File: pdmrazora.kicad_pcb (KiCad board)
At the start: 2 copper layers, 174 x 202 mm, 54 parts, among them J1 6473418-1, J2 M6_VBAT, J3 M6_GND, M1000 Module:mega-mcu144/0.7, U1 BTS50010-1TAD, U11 BTS7004-1EPP, U12 BTS7004-1EPP, U13 BTS7004-1EPP, U14 BTS7004-1EPP, U15 BTS7004-1EPP, U16 BTS7004-1EPP, U17 BTS7004-1EPP, U18 BTS7004-1EPP, U2 BTS50010-1TAD, U3 BTS50010-1TAD, U4 BTS50010-1TAD

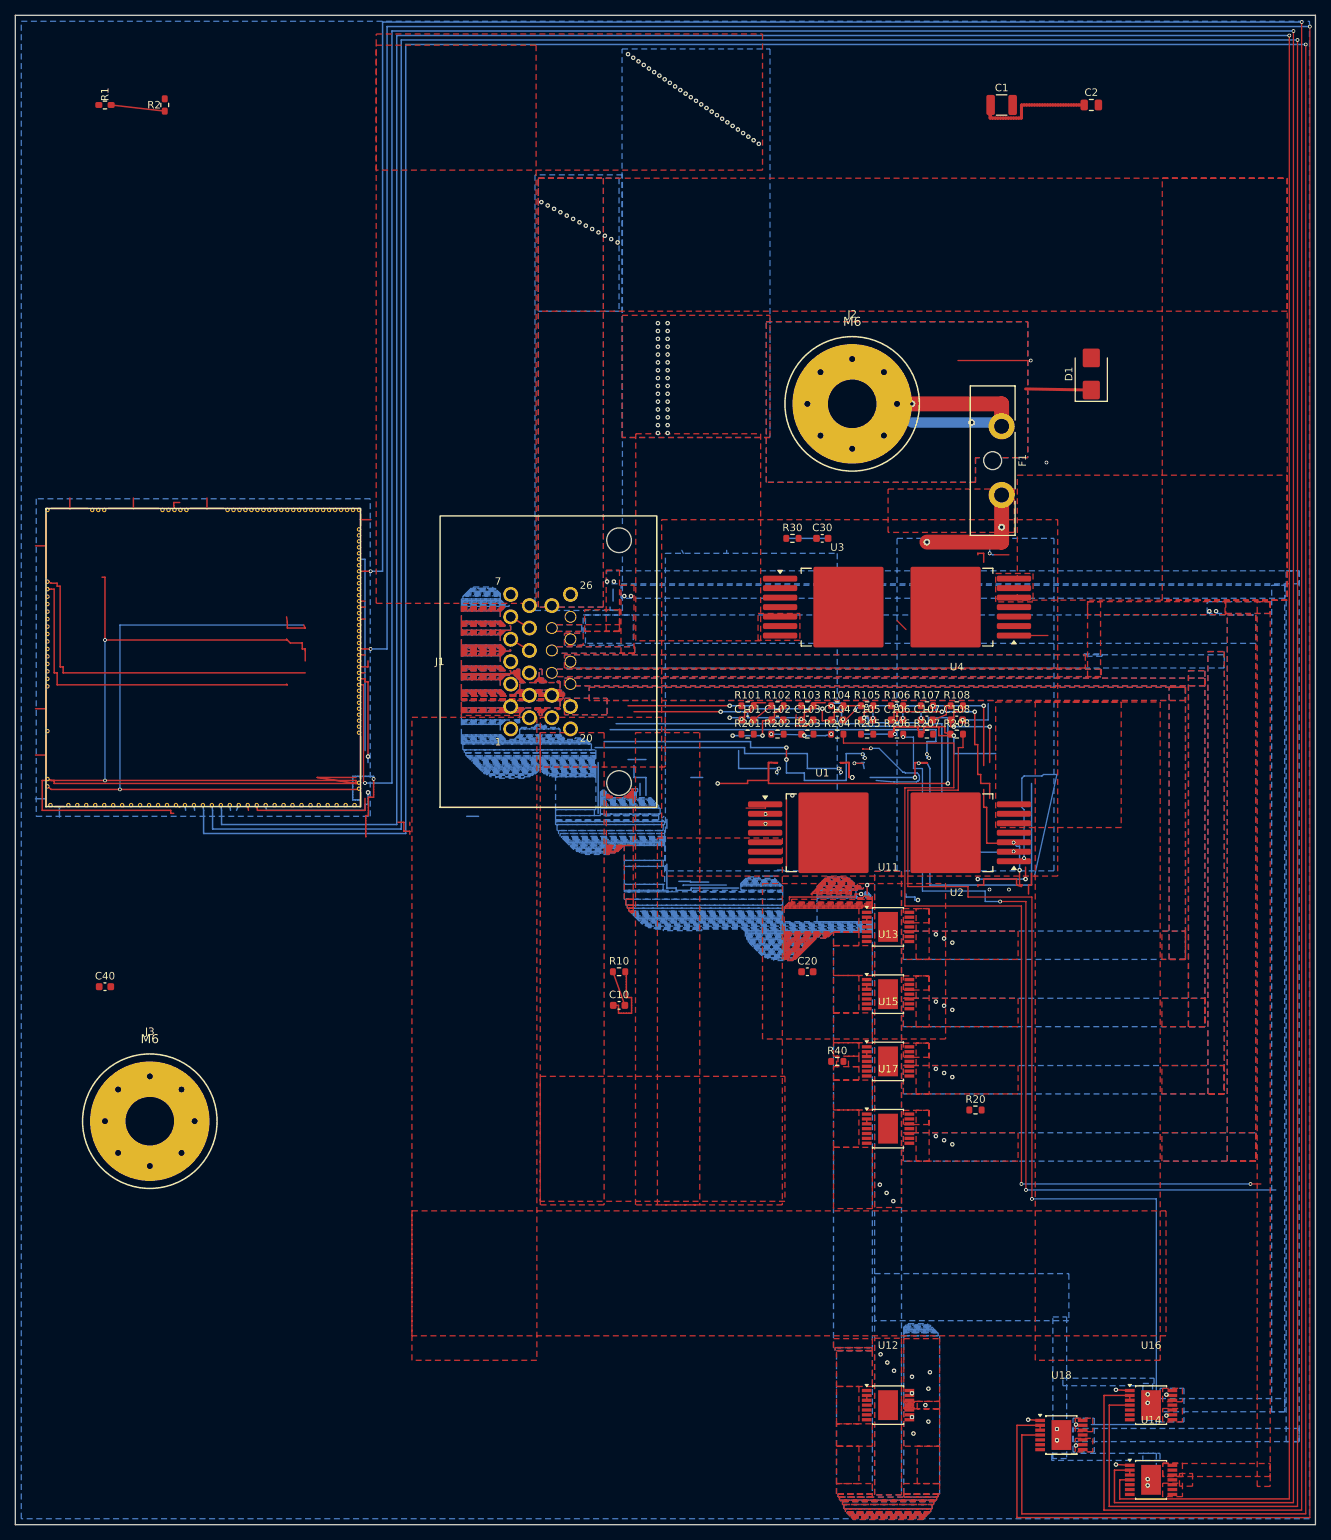
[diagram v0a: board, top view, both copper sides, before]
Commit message: Drop even ADIO channels to 4 HP + 4 low-current outputs. (#28)
Remove ADIO2/4/6/8 drivers, sense parts, and pours, leave their SuperSeal pins no-connect, and keep the odd 8 A necks and the HP pours. Rewire J1 so schematic pin numbers match the loom, and stop the odd pull-ups from merging SENSOR_5V into IO2.

Co-authored-by: Cursor Agent <cursoragent@cursor.com>
Co-authored-by: Quintin <quintinbannink42@users.noreply.github.com>
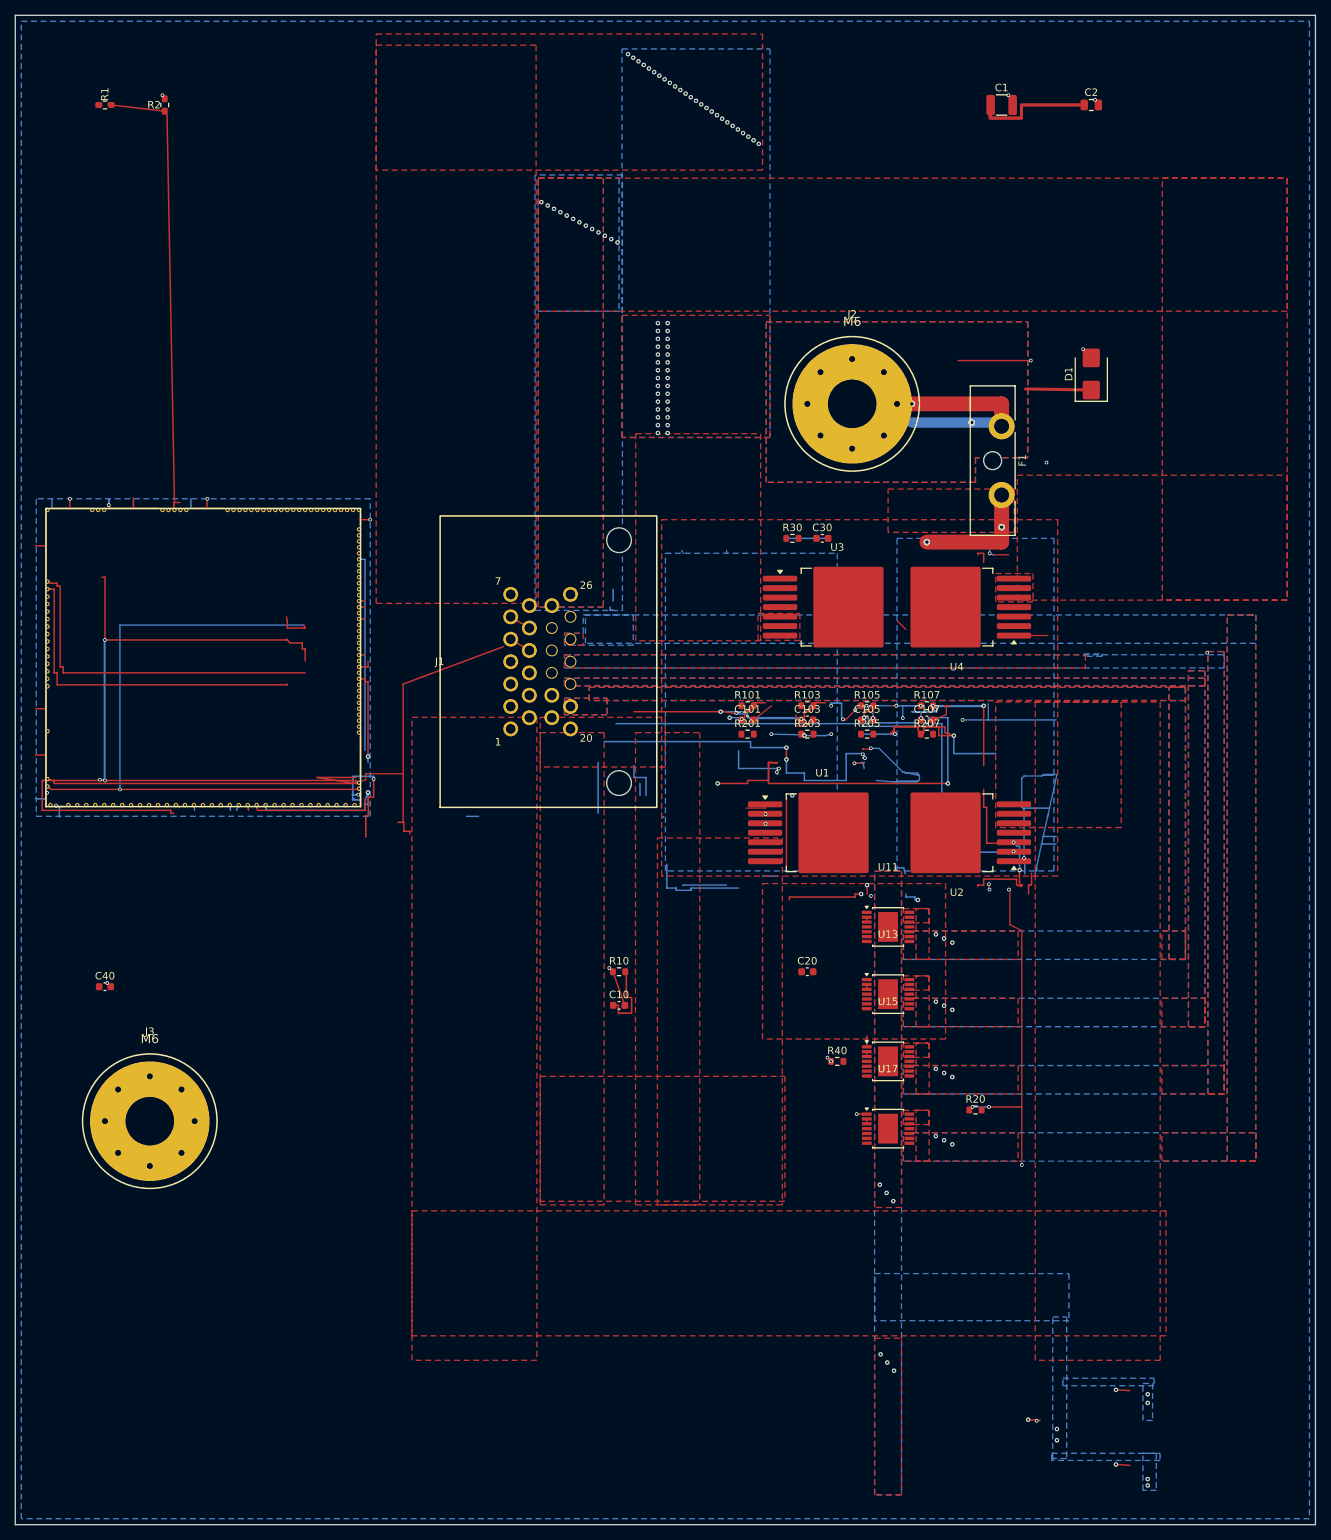
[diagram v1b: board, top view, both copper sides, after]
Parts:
- removed C102, C104, C106, C108: 10n, C_0603_1608Metric
- removed R102, R104, R106, R108, R202, R204, R206, R208: 4k7, R_0603_1608Metric
- removed U12, U14, U16, U18: BTS7004-1EPP, Package_SO:Infineon_PG-TSDSO-14-22
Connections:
- J1 pad 15: ADIO2 -> (no net)
- J1 pad 16: ADIO4 -> (no net)
- J1 pad 17: ADIO6 -> (no net)
- J1 pad 18: ADIO8 -> (no net)
- J1 pad 2: ADIO2 -> (no net)
- J1 pad 9: ADIO2 -> (no net)
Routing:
- net IN_RES3: track 574.8 -> 0.00 mm, vias 5 -> 0
- net IN_RES1: track 536.8 -> 0.00 mm, vias 7 -> 0
- net IN_O2S: track 517.0 -> 0.00 mm, vias 3 -> 0
- net OUT_IO8: track 515.0 -> 0.00 mm, vias 4 -> 0
- net OUT_IO6: track 482.6 -> 0.00 mm, vias 4 -> 0
- net OUT_PWM8: track 466.8 -> 0.00 mm, vias 2 -> 0
- net ADIO8: track 141.7 -> 0.00 mm, vias 5 -> 0
- net ADIO4: track 129.2 -> 0.00 mm, vias 4 -> 0
- net ADIO6: track 110.9 -> 0.00 mm, vias 7 -> 0
- net GND: track 162.7 -> 245.0 mm, vias 19 -> 42
- net SENSOR_5V: track 237.9 -> 296.2 mm, vias 9 -> 10
- net IN_VIGN: track 9.03 -> 60.8 mm
- net IN_MAP2: track 13.1 -> 0.00 mm, vias 2 -> 0
- net IN_MAP3: track 46.6 -> 57.3 mm, vias 2 -> 3
- net IN_RES2: track 45.1 -> 51.5 mm, vias 5 -> 6
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- removed copper zone on B.Cu, net ADIO2
- removed copper zone on F.Cu, net ADIO2
- removed copper zone on B.Cu, net ADIO4
- removed copper zone on F.Cu, net ADIO4
- removed copper zone on B.Cu, net ADIO6
- removed copper zone on F.Cu, net ADIO6
- removed copper zone on B.Cu, net ADIO8
- removed copper zone on F.Cu, net ADIO8
